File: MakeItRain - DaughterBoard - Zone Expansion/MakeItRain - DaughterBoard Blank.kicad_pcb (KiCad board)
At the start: 4 copper layers, 121.3 x 68.1 mm, 1 part, among them J1 Conn_02x15_Odd_Even

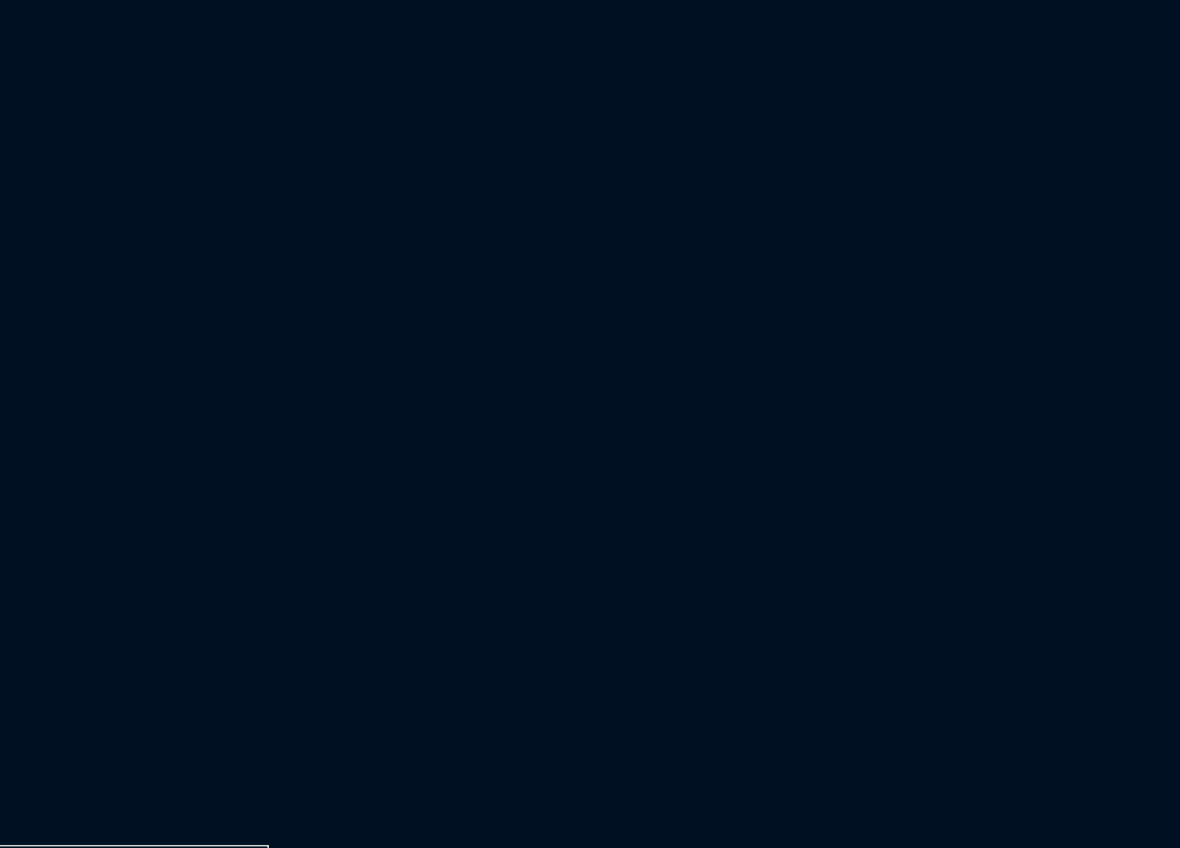
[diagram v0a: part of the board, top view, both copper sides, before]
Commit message: moved fab files into sub folder for main board added to schematics for zones. copy pasta! need to place and route on PCB
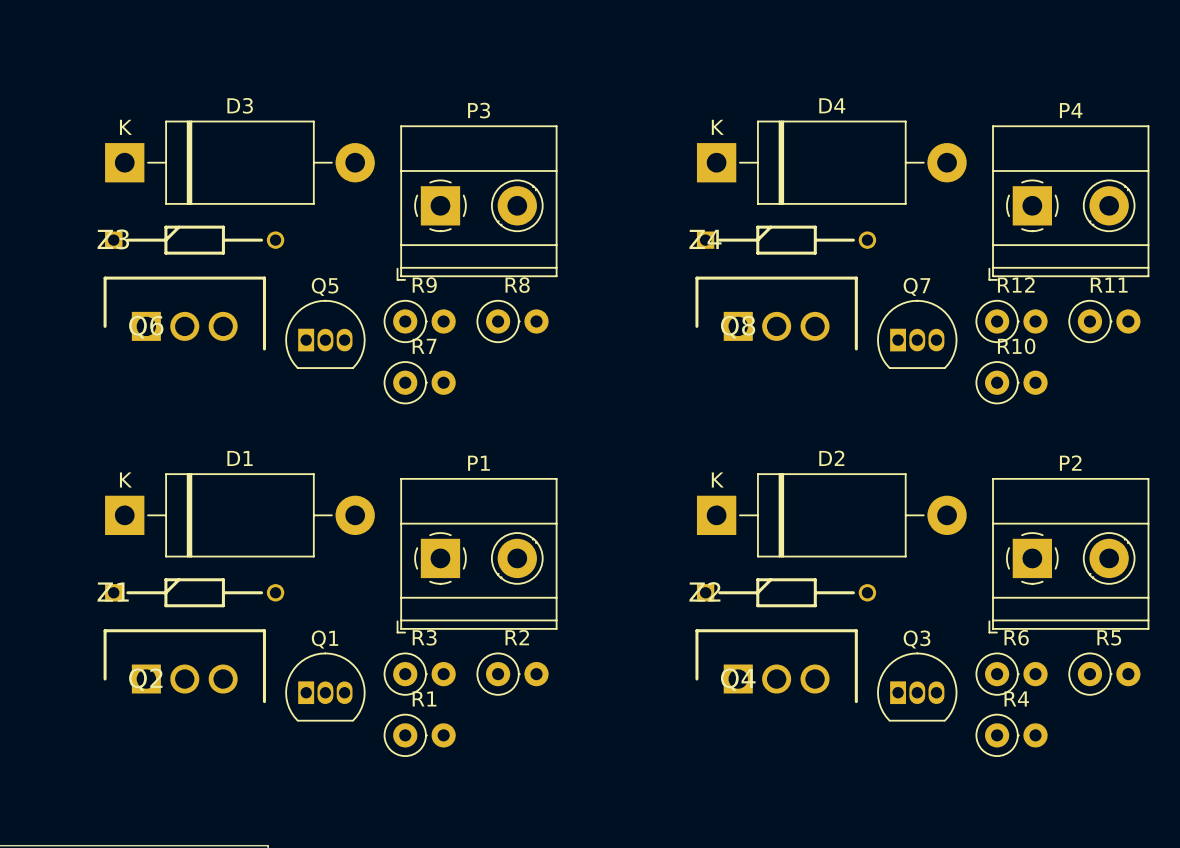
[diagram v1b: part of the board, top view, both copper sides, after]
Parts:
- added D1: STPS3150RL, Diode_THT:D_DO-201_P15.24mm_Horizontal, F.Cu at (163.9, 95.2)
- added D2: STPS3150RL, Diode_THT:D_DO-201_P15.24mm_Horizontal, F.Cu at (203.1, 95.2)
- added D3: STPS3150RL, Diode_THT:D_DO-201_P15.24mm_Horizontal, F.Cu at (163.9, 71.9)
- added D4: STPS3150RL, Diode_THT:D_DO-201_P15.24mm_Horizontal, F.Cu at (203.1, 71.9)
- added P1: Screw_Terminal_01x02, TerminalBlock_Phoenix:TerminalBlock_Phoenix_MKDS-1,5-2-5.08_1x02_P5.08mm_Horizontal, F.Cu at (184.8, 98.1)
- added P2: Screw_Terminal_01x02, TerminalBlock_Phoenix:TerminalBlock_Phoenix_MKDS-1,5-2-5.08_1x02_P5.08mm_Horizontal, F.Cu at (223.9, 98.1)
- added P3: Screw_Terminal_01x02, TerminalBlock_Phoenix:TerminalBlock_Phoenix_MKDS-1,5-2-5.08_1x02_P5.08mm_Horizontal, F.Cu at (184.8, 74.8)
- added P4: Screw_Terminal_01x02, TerminalBlock_Phoenix:TerminalBlock_Phoenix_MKDS-1,5-2-5.08_1x02_P5.08mm_Horizontal, F.Cu at (223.9, 74.8)
- added Q1: 2N7000, Package_TO_SOT_THT:TO-92_Inline, F.Cu at (175.9, 107.0)
- added Q2: IRF9Z34NPBF, SamacSys_Parts:TO254P469X1042X1967-3P, F.Cu at (165.3, 106.1)
- added Q3: 2N7000, Package_TO_SOT_THT:TO-92_Inline, F.Cu at (215.1, 107.0)
- added Q4: IRF9Z34NPBF, SamacSys_Parts:TO254P469X1042X1967-3P, F.Cu at (204.5, 106.1)
- added Q5: 2N7000, Package_TO_SOT_THT:TO-92_Inline, F.Cu at (175.9, 83.7)
- added Q6: IRF9Z34NPBF, SamacSys_Parts:TO254P469X1042X1967-3P, F.Cu at (165.3, 82.8)
- added Q7: 2N7000, Package_TO_SOT_THT:TO-92_Inline, F.Cu at (215.1, 83.7)
- added Q8: IRF9Z34NPBF, SamacSys_Parts:TO254P469X1042X1967-3P, F.Cu at (204.5, 82.8)
- added R1: 1M, Resistor_THT:R_Axial_DIN0207_L6.3mm_D2.5mm_P2.54mm_Vertical, F.Cu at (182.5, 109.8)
- added R10: 1M, Resistor_THT:R_Axial_DIN0207_L6.3mm_D2.5mm_P2.54mm_Vertical, F.Cu at (221.6, 86.5)
- added R11: 100k, Resistor_THT:R_Axial_DIN0207_L6.3mm_D2.5mm_P2.54mm_Vertical, F.Cu at (227.7, 82.4)
- added R12: 10k, Resistor_THT:R_Axial_DIN0207_L6.3mm_D2.5mm_P2.54mm_Vertical, F.Cu at (221.6, 82.4)
- added R2: 100k, Resistor_THT:R_Axial_DIN0207_L6.3mm_D2.5mm_P2.54mm_Vertical, F.Cu at (188.6, 105.7)
- added R3: 10k, Resistor_THT:R_Axial_DIN0207_L6.3mm_D2.5mm_P2.54mm_Vertical, F.Cu at (182.5, 105.7)
- added R4: 1M, Resistor_THT:R_Axial_DIN0207_L6.3mm_D2.5mm_P2.54mm_Vertical, F.Cu at (221.6, 109.8)
- added R5: 100k, Resistor_THT:R_Axial_DIN0207_L6.3mm_D2.5mm_P2.54mm_Vertical, F.Cu at (227.7, 105.7)
- added R6: 10k, Resistor_THT:R_Axial_DIN0207_L6.3mm_D2.5mm_P2.54mm_Vertical, F.Cu at (221.6, 105.7)
- added R7: 1M, Resistor_THT:R_Axial_DIN0207_L6.3mm_D2.5mm_P2.54mm_Vertical, F.Cu at (182.5, 86.5)
- added R8: 100k, Resistor_THT:R_Axial_DIN0207_L6.3mm_D2.5mm_P2.54mm_Vertical, F.Cu at (188.6, 82.4)
- added R9: 10k, Resistor_THT:R_Axial_DIN0207_L6.3mm_D2.5mm_P2.54mm_Vertical, F.Cu at (182.5, 82.4)
- added Z1: BZX79C10, SamacSys_Parts:DIOAD1068W53L380D172, F.Cu at (163.2, 100.4)
- added Z2: BZX79C10, SamacSys_Parts:DIOAD1068W53L380D172, F.Cu at (202.3, 100.4)
- added Z3: BZX79C10, SamacSys_Parts:DIOAD1068W53L380D172, F.Cu at (163.2, 77.0)
- added Z4: BZX79C10, SamacSys_Parts:DIOAD1068W53L380D172, F.Cu at (202.3, 77.0)

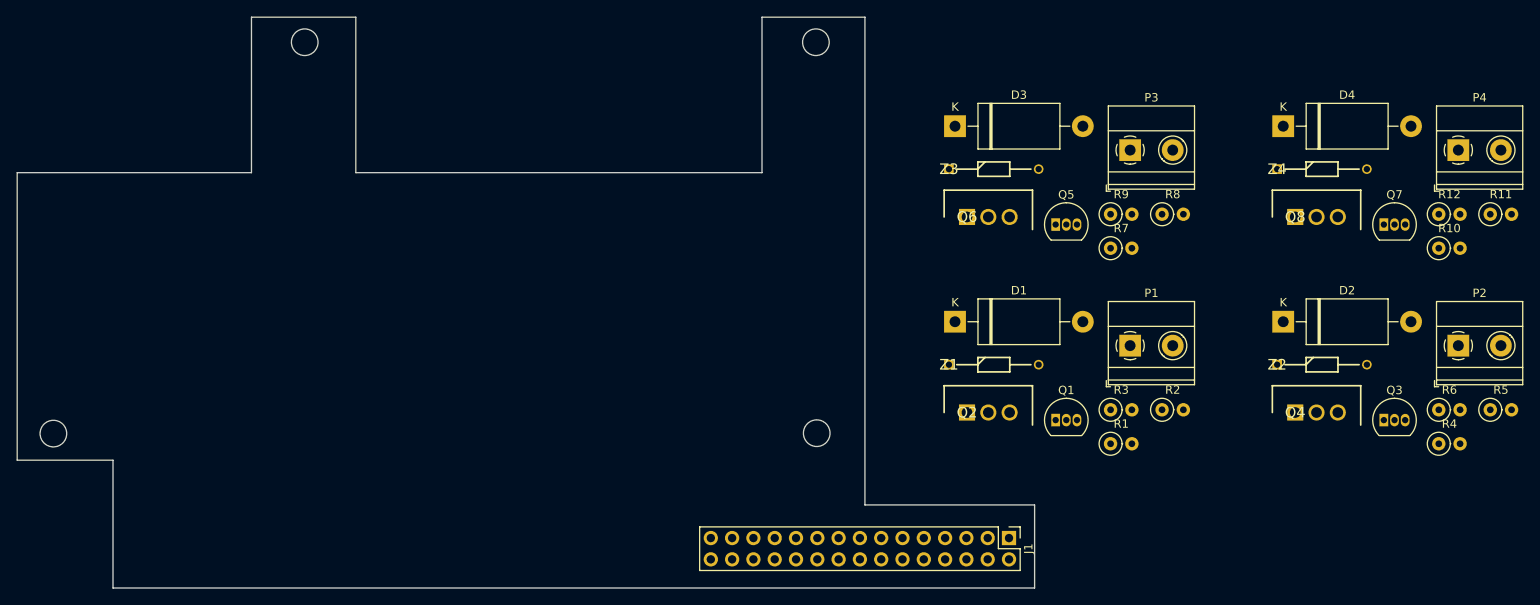
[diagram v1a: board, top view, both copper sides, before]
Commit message: adding support for Zone Expansion daughter board to FW finished daughter board design and pcb layout added fab files for zone expansion daughter board
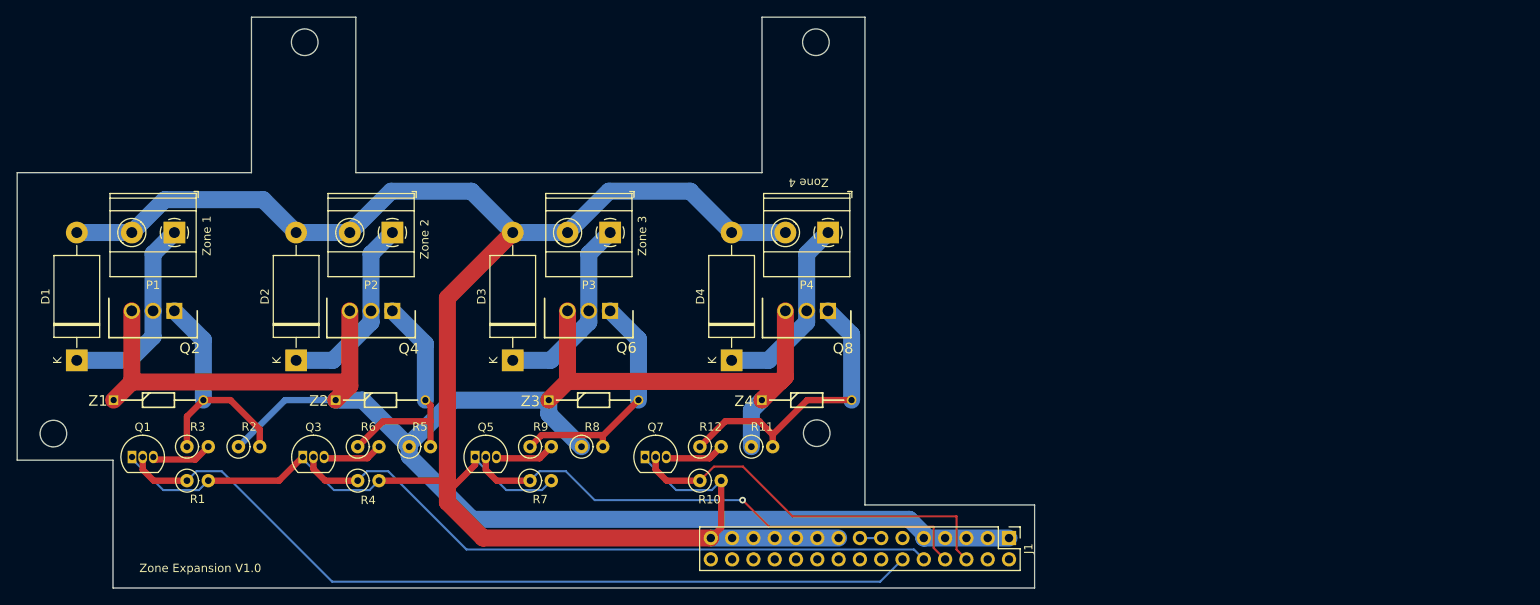
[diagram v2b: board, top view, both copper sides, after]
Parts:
- moved R5 129.0 mm to (98.8, 110.1)
- moved Q3 129.0 mm to (86.1, 111.4)
- moved R4 129.0 mm to (92.7, 114.2)
- moved R6 129.0 mm to (92.7, 110.1)
- moved P2 127.8 mm to (96.8, 84.6), turned to 180 degrees
- moved D2 117.8 mm to (85.3, 99.9), turned to 90 degrees
- moved P1 114.8 mm to (70.8, 84.6), turned to 180 degrees
- moved Z2 112.4 mm to (90.0, 104.6)
- moved R1 110.2 mm to (72.3, 114.2)
- moved R3 110.2 mm to (72.3, 110.1)
- moved Q1 110.2 mm to (65.8, 111.4)
- moved R2 110.2 mm to (78.5, 110.1)
- moved Q4 108.4 mm to (96.8, 93.9), turned to 180 degrees
- moved D1 104.8 mm to (59.2, 99.9), turned to 90 degrees
- moved Z1 99.7 mm to (63.6, 104.6)
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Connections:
- Q1 pad 2: D23 -> D5
- Q3 pad 2: D19 -> D18
- Q5 pad 2: D18 -> D19
- Q7 pad 2: D5 -> D23
- R1 pad 1: D23 -> D5
- R10 pad 1: D5 -> D23
- R4 pad 1: D19 -> D18
- R7 pad 1: D18 -> D19
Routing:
- net GND: track 0.00 -> 258.8 mm
- net +VDC: track 0.00 -> 233.0 mm
- net D5: track 0.00 -> 99.7 mm
- net D18: track 0.00 -> 79.6 mm
- net D19: track 0.00 -> 63.1 mm, vias 0 -> 1
- net D23: track 0.00 -> 46.7 mm
- net Net-(Q8-Pad1): track 0.00 -> 35.0 mm
- net Net-(Q2-Pad1): track 0.00 -> 28.7 mm
- net Net-(Q6-Pad1): track 0.00 -> 28.6 mm
- net Net-(Q4-Pad1): track 0.00 -> 28.0 mm
- net Net-(D1-Pad1): track 0.00 -> 23.7 mm
- net Net-(D3-Pad1): track 0.00 -> 22.7 mm
- net Net-(D4-Pad1): track 0.00 -> 22.6 mm
- net Net-(D2-Pad1): track 0.00 -> 22.6 mm
- net Net-(Q1-Pad3): track 0.00 -> 7.31 mm
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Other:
- copper layers 4 -> 2
- board text added: "Zone 1"
- board text added: "Zone 2"
- board text added: "Zone 3"
- board text added: "Zone 4"
- board text added: "Zone Expansion V1.0"

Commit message: updating some routes, updating the already done daughterboard and updating the blank layout for both.
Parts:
- J1: value Conn_02x15_Odd_Even -> Conn_02x14_Odd_Even; footprint Connector_PinHeader_2.54mm:PinHeader_2x15_P2.54mm_Vertical -> Connector_PinHeader_2.54mm:PinHeader_2x14_P2.54mm_Vertical
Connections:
- net AuxVoltage renamed SDA
- net D21 renamed D17
- net D35 renamed D26
- net D39 renamed SCL
- net D4 renamed D16
- J1 pad 10: D18 -> Z6
- J1 pad 12: D5 -> Z5
- J1 pad 13: +5V -> +3V3
- J1 pad 15: +5V -> +3V3
- J1 pad 16: D32 -> D23
- J1 pad 17: GND -> +3V3
- J1 pad 18: D33 -> D19
- J1 pad 20: D25 -> D18
- J1 pad 26: D0 -> TX
- J1 pad 28: TX -> RX
- J1 pad 6: D23 -> Z8
- J1 pad 8: D19 -> Z7
- Q1 pad 2: D5 -> /Output/TTL
- Q3 pad 2: D18 -> /Output1/TTL
- Q5 pad 2: D19 -> /Output2/TTL
- Q7 pad 2: D23 -> /Output3/TTL
- R1 pad 1: D5 -> /Output/TTL
- R10 pad 1: D23 -> /Output3/TTL
- R4 pad 1: D18 -> /Output1/TTL
- R7 pad 1: D19 -> /Output2/TTL
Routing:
- net D5: track 99.7 -> 0.00 mm
- net /Output/TTL: track 0.00 -> 99.7 mm
- net D18: track 79.6 -> 0.00 mm
- net /Output1/TTL: track 0.00 -> 79.6 mm
- net D19: track 63.1 -> 0.00 mm, vias 1 -> 0
- net /Output2/TTL: track 0.00 -> 63.1 mm, vias 0 -> 1
- net D23: track 46.7 -> 0.00 mm
- net /Output3/TTL: track 0.00 -> 46.7 mm
- net +5V: track 2.54 -> 0.00 mm
- net +3V3: track 0.00 -> 2.54 mm
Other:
- board text added: "Zone 5"
- board text added: "Zone 6"
- board text added: "Zone 7"
- board text added: "Zone 8"
- board text removed: "Zone 1"
- board text removed: "Zone 2"
- board text removed: "Zone 3"
- board text removed: "Zone 4"

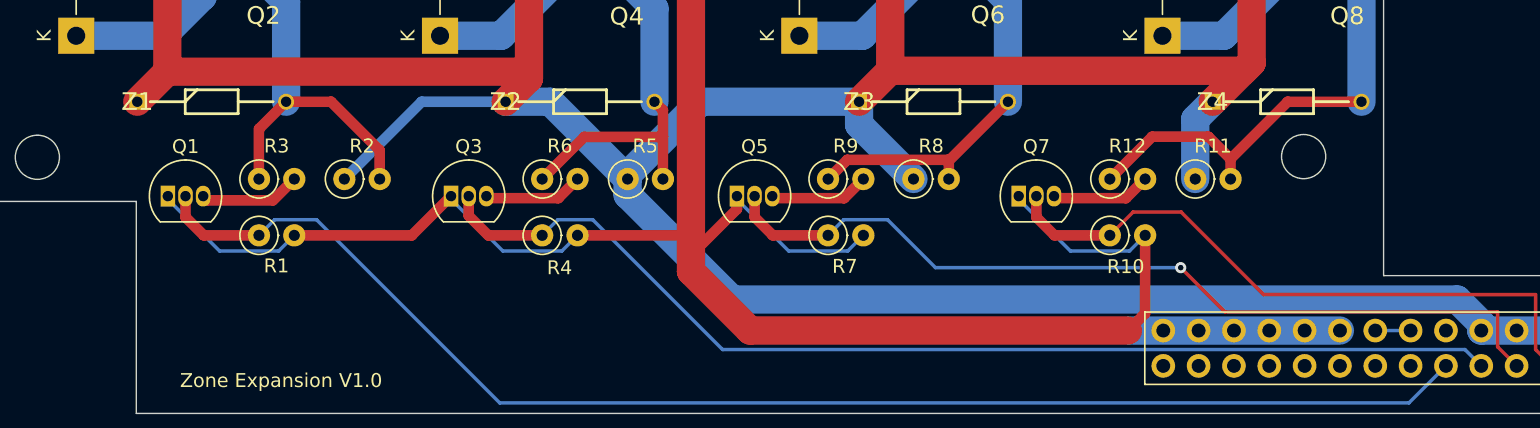
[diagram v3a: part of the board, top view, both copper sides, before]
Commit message: MakeItRain * Main Board Fixed Routing. * replaced Opamp with the part that i can get as the old one is EOL * generated all the fab files i need. * updated the daughter plug witht eh i2c ttl flip * fixed I2C issues * DRC'ed the board
MakeItRain - DaughterBoard - Zone Expansion
* updated the daughter plug witht eh i2c ttl flip
* fixed some of the routings
* generated new fab files
* DRC'ed the board
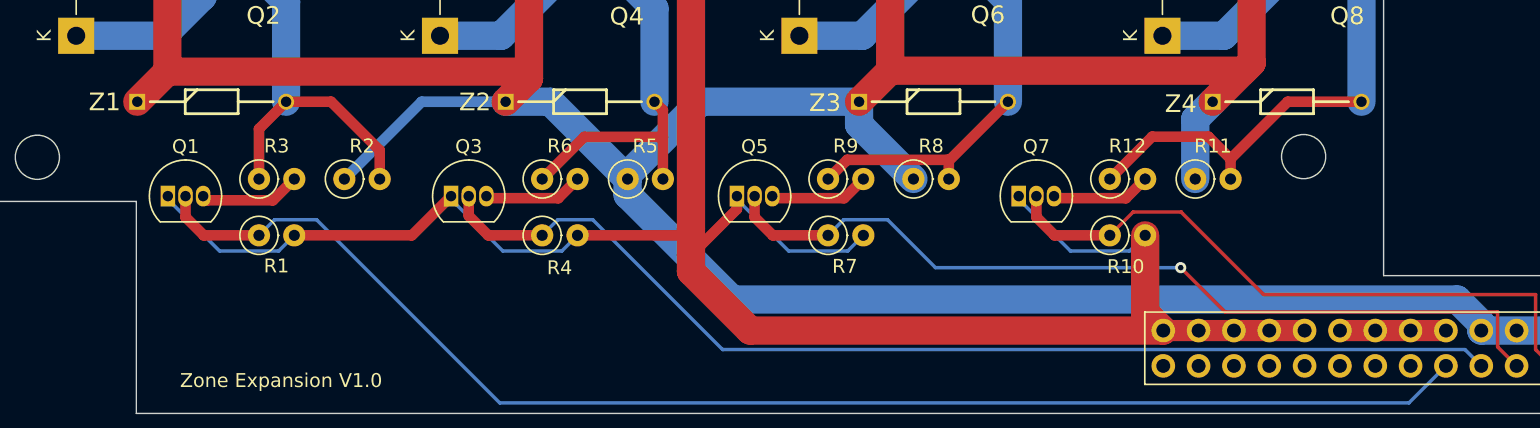
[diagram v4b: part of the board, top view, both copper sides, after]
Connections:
- J1 pad 2: SCL -> TX
- J1 pad 26: TX -> SCL
- J1 pad 28: RX -> SDA
- J1 pad 4: SDA -> RX
- Q1 pad 2: /Output/TTL -> Z5
- Q3 pad 2: /Output1/TTL -> Z6
- Q5 pad 2: /Output2/TTL -> Z7
- Q7 pad 2: /Output3/TTL -> Z8
- R1 pad 1: /Output/TTL -> Z5
- R10 pad 1: /Output3/TTL -> Z8
- R4 pad 1: /Output1/TTL -> Z6
- R7 pad 1: /Output2/TTL -> Z7
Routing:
- net Z5: track 0.00 -> 99.7 mm
- net /Output/TTL: track 99.7 -> 0.00 mm
- net Z6: track 0.00 -> 79.6 mm
- net /Output1/TTL: track 79.6 -> 0.00 mm
- net Z7: track 0.00 -> 63.1 mm, vias 0 -> 1
- net /Output2/TTL: track 63.1 -> 0.00 mm, vias 1 -> 0
- net Z8: track 0.00 -> 46.7 mm
- net /Output3/TTL: track 46.7 -> 0.00 mm
- net +3V3: track 2.54 -> 7.62 mm
- net GND: track 258.8 -> 255.4 mm
